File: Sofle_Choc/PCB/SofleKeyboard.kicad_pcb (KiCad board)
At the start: 2 copper layers, 143.4 x 111.8 mm, 84 parts, among them J2 4PIN, J3 OLED, P1 i2c_pin, P2 i2c_pin, SW1 SW_PUSH_LED, SW10 SW_PUSH_LED, SW11 SW_PUSH_LED, SW12 SW_PUSH_LED, SW13 SW_PUSH_LED, SW14 SW_PUSH_LED, SW15 SW_PUSH_LED, SW16 SW_PUSH_LED, SW17 SW_PUSH_LED, SW18 SW_PUSH_LED, SW19 SW_PUSH_LED, SW2 SW_PUSH_LED, SW20 SW_PUSH_LED, SW21 SW_PUSH_LED, SW22 SW_PUSH_LED, SW23 SW_PUSH_LED, SW24 SW_PUSH_LED, SW25 Rotary_Encoder_Switch, SW26 SW_PUSH_LED, SW27 SW_PUSH_LED, SW28 SW_PUSH_LED, SW29 SW_PUSH_LED, SW3 SW_PUSH_LED, SW30 SW_PUSH_LED, SW4 SW_PUSH_LED, SW5 SW_PUSH_LED, SW6 SW_PUSH_LED, SW7 SW_PUSH_LED, SW8 SW_PUSH_LED, SW9 SW_PUSH_LED, U1 ProMicro

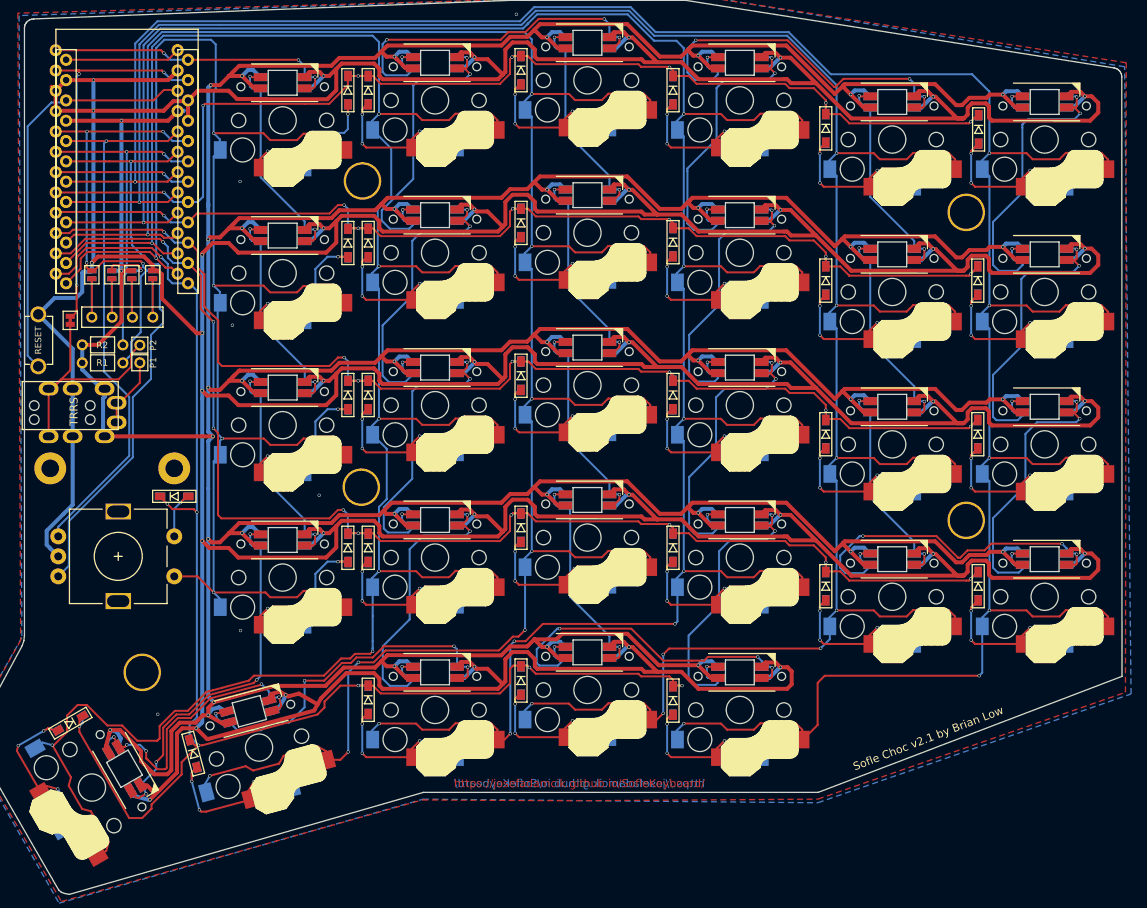
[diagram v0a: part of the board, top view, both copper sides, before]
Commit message: Fix footprints
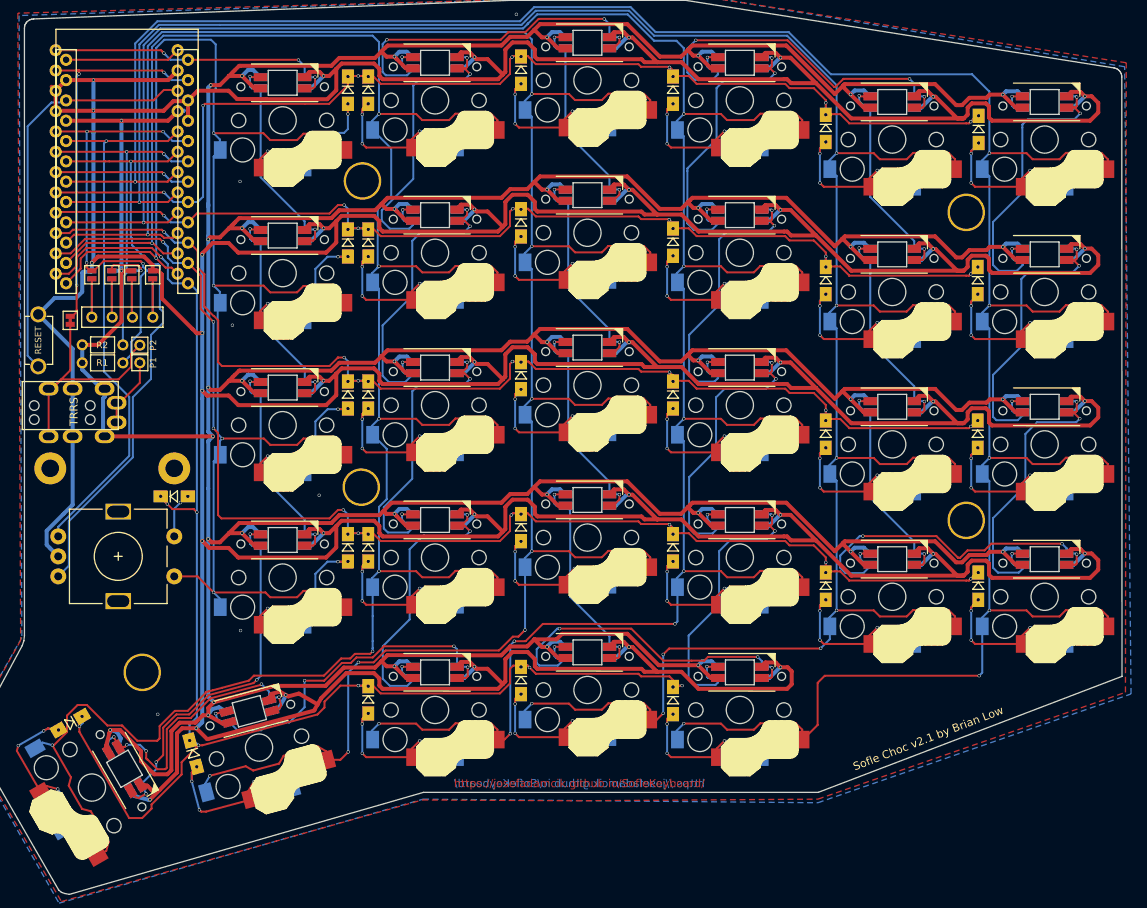
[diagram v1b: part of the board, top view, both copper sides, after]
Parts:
- D1, D10, D11, D12, D13, D14, D15, D16, D17, D18, D19, D2, D20, D21, D22, D23, D24, D25, D26, D27, D28, D29, D3, D30, D4, D5, D6, D7, D8, D9: footprint Diode_SMD:crkbd-diode -> SofleKeyboard-footprint:Diode_SOD123
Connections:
- SW6 pad 2: Net-(SW6-Pad2) -> unconnected-(SW6B-DOUT-Pad2)
- U1 pad 24: Net-(U1-Pad24) -> unconnected-(U1-RAW-Pad24)
- U1 pad 7: Net-(U1-Pad7) -> unconnected-(U1-D4(PD4)-Pad7)
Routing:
- net Net-(D26-Pad2): track 0.00 -> 22.6 mm, vias 0 -> 3
- net Net-(D26-A): track 22.6 -> 0.00 mm, vias 3 -> 0
- net Net-(U1-Pad7): track 17.0 -> 0.00 mm, vias 1 -> 0
- net unconnected-(U1-D4(PD4)-Pad7): track 0.00 -> 17.0 mm, vias 0 -> 1
- net unconnected-(U1-RAW-Pad24): track 0.00 -> 14.4 mm
- net Net-(U1-Pad24): track 14.4 -> 0.00 mm
- net unconnected-(SW6B-DOUT-Pad2): track 0.00 -> 3.91 mm, vias 0 -> 1
- net Net-(SW6-Pad2): track 3.91 -> 0.00 mm, vias 1 -> 0
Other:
- net class Default removed
- net class GND removed
- net class VCC removed

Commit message: Add 7th row and move thumb cluster
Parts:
- removed the D30 at (169.3, 122.5)
- removed the SW30 at (177.7, 123.7)
- added D26: D, SofleKeyboard-footprint:Diode_SOD123, F.Cu at (77.4, 134.9)
- added D31: D, SofleKeyboard-footprint:Diode_SOD123, F.Cu at (226.4, 51.0)
- added D32: D, SofleKeyboard-footprint:Diode_SOD123, F.Cu at (226.4, 70.4)
- added D33: D, SofleKeyboard-footprint:Diode_SOD123, F.Cu at (226.4, 88.8)
- added D34: D, SofleKeyboard-footprint:Diode_SOD123, F.Cu at (226.4, 108.2)
- added D35: D, SofleKeyboard-footprint:Diode_SOD123, F.Cu at (226.6, 127.2)
- added SW26: SW_PUSH_LED, SofleChoc:Choc_Hotswap_SK6812MiniE, F.Cu at (80.1, 142.9)
- added SW31: SW_PUSH_LED, SofleChoc:Choc_Hotswap_SK6812MiniE, F.Cu at (234.8, 52.4)
- added SW32: SW_PUSH_LED, SofleChoc:Choc_Hotswap_SK6812MiniE, F.Cu at (234.8, 71.5)
- added SW33: SW_PUSH_LED, SofleChoc:Choc_Hotswap_SK6812MiniE, F.Cu at (234.8, 90.5)
- added SW34: SW_PUSH_LED, SofleChoc:Choc_Hotswap_SK6812MiniE, F.Cu at (234.8, 109.5)
- added SW35: SW_PUSH_LED, SofleChoc:Choc_Hotswap_SK6812MiniE, F.Cu at (234.8, 128.6)
- renumbered D26 to D27, D27 to D28, D28 to D29, D29 to D30, SW26 to SW27, SW27 to SW28, SW28 to SW29, SW29 to SW30
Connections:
- SW27 pad 4: Net-(SW19B-DOUT) -> Net-(SW26B-DOUT)
- SW27 pad 6: col4 -> col3
- SW28 pad 2: Net-(SW27B-DOUT) (its old number) -> Net-(SW20B-DIN)
- SW28 pad 6: col3 -> col2
- SW29 pad 2: Net-(SW20B-DIN) -> Net-(SW29B-DOUT)
- SW29 pad 4: Net-(SW27B-DOUT) (its old number) -> Net-(SW21B-DOUT)
- SW29 pad 6: col2 -> col1
- SW30 pad 2: Net-(SW29B-DOUT) -> Net-(SW22B-DIN)
- SW30 pad 4: Net-(SW21B-DOUT) -> Net-(SW29B-DOUT)
- SW30 pad 6: col1 -> col0
- SW6 pad 2: unconnected-(SW6B-DOUT-Pad2) -> Net-(SW31B-DIN)
- U1 pad 7: unconnected-(U1-D4(PD4)-Pad7) -> col6
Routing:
- net Net-(SW29B-DOUT): track 45.5 -> 0.00 mm, vias 4 -> 0
- net (no net): track 0.00 -> 45.3 mm, vias 0 -> 6
- net Net-(SW27B-DOUT) (its old number): track 44.9 -> 0.00 mm, vias 4 -> 0
- net Net-(SW27B-DOUT): track 36.6 -> 81.6 mm, vias 5 -> 9
- net col4: track 288.6 -> 319.2 mm, vias 7 -> 8
- net col1: track 317.4 -> 287.4 mm, vias 9 -> 6
- net GND: track 1090.4 -> 1066.4 mm, vias 43 -> 42
- net Net-(D30-A) (its old number): track 22.6 -> 0.00 mm, vias 3 -> 0
- net Net-(D26-Pad2): track 22.6 -> 0.00 mm, vias 3 -> 0
- net unconnected-(U1-D4(PD4)-Pad7): track 17.0 -> 0.00 mm, vias 1 -> 0
- net col6: track 0.00 -> 17.0 mm, vias 0 -> 1
- net Net-(SW22B-DIN): track 39.9 -> 54.1 mm, vias 3 -> 4
- net row4: track 189.5 -> 203.6 mm
- net VCC: track 889.9 -> 884.1 mm, vias 37 -> 36
- net col0: track 336.6 -> 331.0 mm
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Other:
- board size 143.4 x 111.8 mm -> 179.3 x 122 mm
- board text added: "s31"
- board text added: "s32"
- board text added: "s33"
- board text added: "s34"
- board text added: "s35"
- board text removed: "Sofle Choc v2.1 by Brian Low"

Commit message: Fix routes
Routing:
- net col6: track 17.0 -> 308.4 mm, vias 1 -> 10
- net GND: track 1066.4 -> 1250.2 mm, vias 42 -> 47
- net VCC: track 884.1 -> 1063.3 mm, vias 36 -> 41
- net row4: track 203.6 -> 264.7 mm
- net col1: track 287.4 -> 339.5 mm, vias 6 -> 9
- net Net-(SW31B-DIN): track 3.91 -> 44.5 mm, vias 1 -> 4
- net Net-(SW34B-DOUT): track 0.00 -> 31.9 mm, vias 0 -> 2
- net Net-(SW33B-DOUT): track 0.00 -> 31.8 mm, vias 0 -> 2
- net Net-(SW31B-DOUT): track 0.00 -> 29.9 mm, vias 0 -> 2
- net Net-(SW32B-DOUT): track 0.00 -> 28.7 mm, vias 0 -> 2
- net col0: track 331.0 -> 359.2 mm
- net row2: track 147.9 -> 170.8 mm, vias 7 -> 8
- net Net-(D31-A): track 0.00 -> 22.6 mm, vias 0 -> 3
- net Net-(D34-A): track 0.00 -> 22.2 mm, vias 0 -> 3
- net row3: track 166.8 -> 188.8 mm, vias 9 -> 10
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
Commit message: Add routing
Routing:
- net Net-(SW27B-DOUT): track 81.6 -> 26.5 mm, vias 9 -> 1
- net col2: track 285.0 -> 335.6 mm, vias 8 -> 7
- net (no net): track 45.3 -> 0.00 mm, vias 6 -> 0
- net Net-(SW29B-DOUT): track 0.00 -> 37.1 mm, vias 0 -> 1
- net col3: track 290.9 -> 326.3 mm, vias 9 -> 8
- net Net-(SW19B-DOUT): track 47.0 -> 77.3 mm
- net Net-(SW26B-DOUT): track 0.00 -> 25.5 mm, vias 0 -> 1
- net GND: track 1250.2 -> 1273.6 mm
- net Net-(D27-A): track 0.00 -> 23.0 mm, vias 0 -> 3
- net Net-(SW21B-DOUT): track 27.6 -> 48.0 mm, vias 2 -> 4
- net Net-(D26-A): track 0.00 -> 20.1 mm, vias 0 -> 2
- net Net-(SW20B-DIN): track 40.0 -> 60.1 mm, vias 3 -> 4
- net VCC: track 1063.3 -> 1080.8 mm
- net col4: track 319.2 -> 311.1 mm
- net Net-(SW22B-DIN): track 54.1 -> 46.9 mm, vias 4 -> 6
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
